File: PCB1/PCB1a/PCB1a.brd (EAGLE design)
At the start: 125.6 x 84.2 mm, 0 parts

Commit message: .
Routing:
- added copper zone on layer 1, net GND
- added copper zone on layer 16, net GND
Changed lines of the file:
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@@
 <setting verticaltext="up"/>
 </settings>
-<grid distance="3.75" unitdist="mm" unit="mm" style="lines" multiple="1" display="yes" altdistance="5" altunitdist="mil" altunit="mil"/>
+<grid distance="4" unitdist="mm" unit="mm" style="lines" multiple="1" display="yes" altdistance="5" altunitdist="mil" altunit="mil"/>
 <layers>
 <layer number="1" name="Top" color="4" fill="1" visible="yes" active="yes"/>
@@
 <layer number="51" name="tDocu" color="7" fill="1" visible="yes" active="yes"/>
 <layer number="52" name="bDocu" color="7" fill="1" visible="yes" active="yes"/>
+<layer number="91" name="Nets" color="2" fill="1" visible="no" active="no"/>
+<layer number="92" name="Busses" color="1" fill="1" visible="no" active="no"/>
+<layer number="93" name="Pins" color="2" fill="1" visible="no" active="no"/>
+<layer number="94" name="Symbols" color="4" fill="1" visible="no" active="no"/>
+<layer number="95" name="Names" color="7" fill="1" visible="no" active="no"/>
+<layer number="96" name="Values" color="7" fill="1" visible="no" active="no"/>
+<layer number="97" name="Info" color="7" fill="1" visible="no" active="no"/>
+<layer number="98" name="Guide" color="6" fill="1" visible="no" active="no"/>
 </layers>
 <board>
@@
 <dimension x1="50.6" y1="42.1" x2="50.6" y2="-42.1" x3="60.6" y3="0" textsize="1.778" layer="47"/>
 <dimension x1="50.6" y1="-42.1" x2="-75" y2="-42.1" x3="-12.2" y3="-52.1" textsize="1.778" layer="47"/>
+<rectangle x1="42.85" y1="34.35" x2="50.6" y2="42.1" layer="41"/>
+<rectangle x1="42.85" y1="34.35" x2="50.6" y2="42.1" layer="42"/>
 </plain>
 <attributes>
@@
 </elements>
 <signals>
-<signal name="S$1">
+<signal name="MOUNT2">
 <via x="46.85" y="38.35" extent="1-16" drill="3.2" diameter="7" locked="yes"/>
 <via x="46.85" y="-38.35" extent="1-16" drill="3.2" diameter="7" locked="yes"/>
@@
 <wire x1="-46.85" y1="38.35" x2="-46.85" y2="-38.35" width="0" layer="19" extent="1-1"/>
 </signal>
+<signal name="GND">
+<polygon width="0.1524" layer="1">
+<vertex x="50.6" y="-42.1"/>
+<vertex x="50.6" y="42.1"/>
+<vertex x="-75" y="42.1"/>
+<vertex x="-75" y="-42.1"/>
+</polygon>
+<polygon width="0.1524" layer="16">
+<vertex x="50.6" y="-42.1"/>
+<vertex x="50.6" y="42.1"/>
+<vertex x="-75" y="42.1"/>
+<vertex x="-75" y="-42.1"/>
+</polygon>
+</signal>
 </signals>

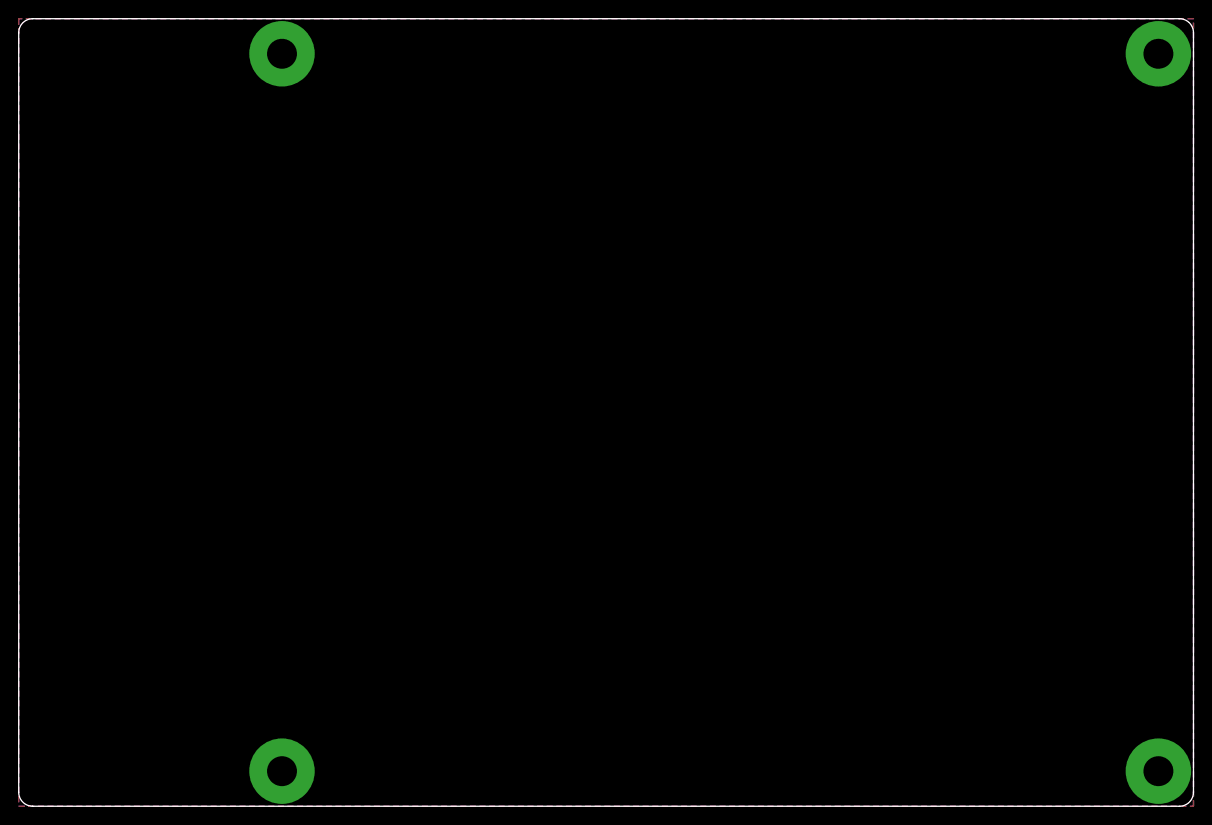
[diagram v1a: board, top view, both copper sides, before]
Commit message: Outline done .
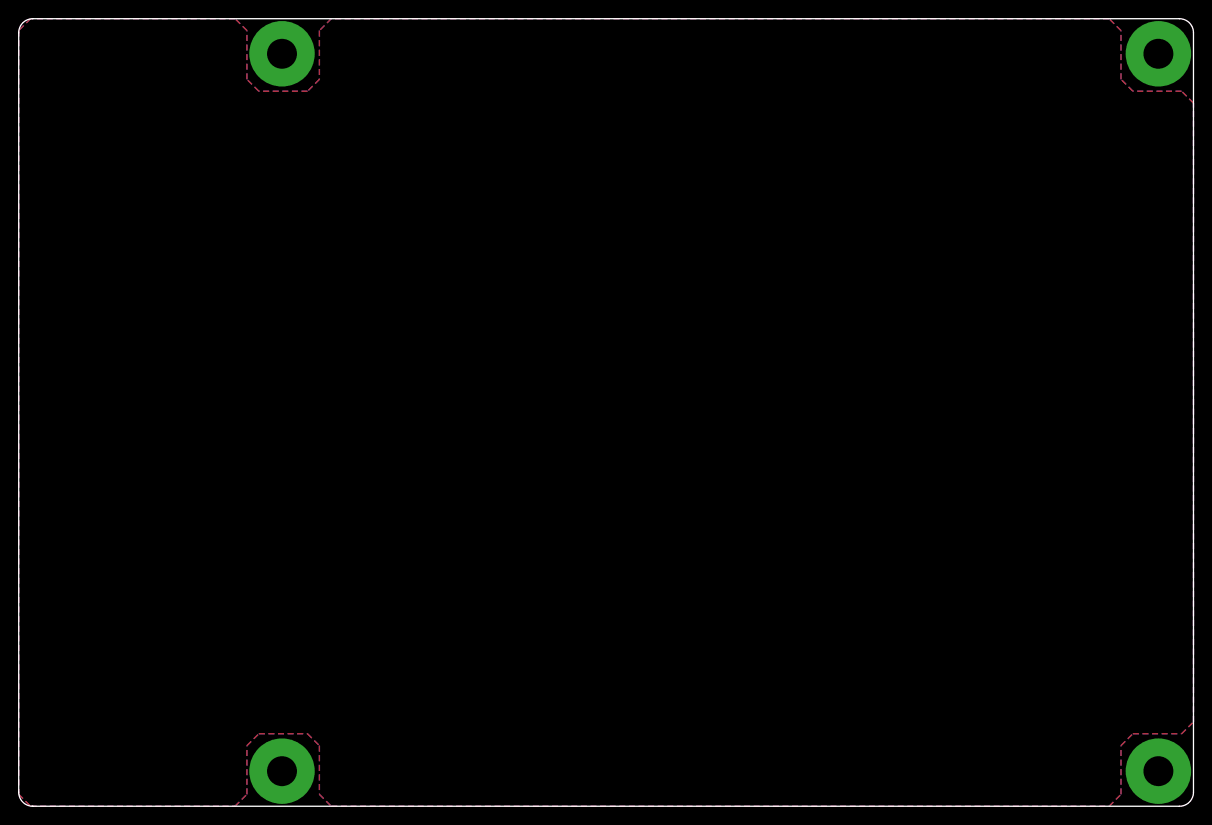
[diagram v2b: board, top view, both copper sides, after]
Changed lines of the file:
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@@
 <drawing>
 <settings>
-<setting alwaysvectorfont="no"/>
+<setting alwaysvectorfont="yes"/>
 <setting verticaltext="up"/>
 </settings>
@@
 <layer number="25" name="tNames" color="7" fill="1" visible="yes" active="yes"/>
 <layer number="26" name="bNames" color="7" fill="1" visible="yes" active="yes"/>
-<layer number="27" name="tValues" color="7" fill="1" visible="yes" active="yes"/>
-<layer number="28" name="bValues" color="7" fill="1" visible="yes" active="yes"/>
+<layer number="27" name="tValues" color="7" fill="1" visible="no" active="yes"/>
+<layer number="28" name="bValues" color="7" fill="1" visible="no" active="yes"/>
 <layer number="29" name="tStop" color="7" fill="3" visible="no" active="yes"/>
 <layer number="30" name="bStop" color="7" fill="6" visible="no" active="yes"/>
@@
 <layer number="41" name="tRestrict" color="4" fill="10" visible="yes" active="yes"/>
 <layer number="42" name="bRestrict" color="1" fill="10" visible="yes" active="yes"/>
-<layer number="43" name="vRestrict" color="2" fill="10" visible="yes" active="yes"/>
+<layer number="43" name="vRestrict" color="2" fill="10" visible="no" active="yes"/>
 <layer number="44" name="Drills" color="7" fill="1" visible="no" active="yes"/>
 <layer number="45" name="Holes" color="7" fill="1" visible="no" active="yes"/>
 <layer number="46" name="Milling" color="3" fill="1" visible="no" active="yes"/>
-<layer number="47" name="Measures" color="7" fill="1" visible="yes" active="yes"/>
-<layer number="48" name="Document" color="7" fill="1" visible="yes" active="yes"/>
-<layer number="49" name="Reference" color="7" fill="1" visible="yes" active="yes"/>
+<layer number="47" name="Measures" color="7" fill="1" visible="no" active="yes"/>
+<layer number="48" name="Document" color="7" fill="1" visible="no" active="yes"/>
+<layer number="49" name="Reference" color="7" fill="1" visible="no" active="yes"/>
 <layer number="51" name="tDocu" color="7" fill="1" visible="yes" active="yes"/>
 <layer number="52" name="bDocu" color="7" fill="1" visible="yes" active="yes"/>
@@
 <board>
 <plain>
-<wire x1="-75" y1="40.6" x2="-75" y2="-40.6" width="0" layer="20"/>
-<wire x1="-75" y1="-40.6" x2="-73.5" y2="-42.1" width="0" layer="20" curve="90"/>
-<wire x1="-73.5" y1="-42.1" x2="49.1" y2="-42.1" width="0" layer="20"/>
-<wire x1="-75" y1="40.6" x2="-73.5" y2="42.1" width="0" layer="20" curve="-90"/>
-<wire x1="49.1" y1="-42.1" x2="50.6" y2="-40.6" width="0" layer="20" curve="90"/>
-<wire x1="50.6" y1="-40.6" x2="50.6" y2="40.6" width="0" layer="20"/>
-<wire x1="50.6" y1="40.6" x2="49.1" y2="42.1" width="0" layer="20" curve="90"/>
-<wire x1="49.1" y1="42.1" x2="-73.5" y2="42.1" width="0" layer="20"/>
+<wire x1="-75" y1="40.6" x2="-75" y2="-40.6" width="0" layer="20" locked="yes"/>
+<wire x1="-75" y1="-40.6" x2="-73.5" y2="-42.1" width="0" layer="20" curve="90" locked="yes"/>
+<wire x1="-73.5" y1="-42.1" x2="49.1" y2="-42.1" width="0" layer="20" locked="yes"/>
+<wire x1="-75" y1="40.6" x2="-73.5" y2="42.1" width="0" layer="20" curve="-90" locked="yes"/>
+<wire x1="49.1" y1="-42.1" x2="50.6" y2="-40.6" width="0" layer="20" curve="90" locked="yes"/>
+<wire x1="50.6" y1="-40.6" x2="50.6" y2="40.6" width="0" layer="20" locked="yes"/>
+<wire x1="50.6" y1="40.6" x2="49.1" y2="42.1" width="0" layer="20" curve="90" locked="yes"/>
+<wire x1="49.1" y1="42.1" x2="-73.5" y2="42.1" width="0" layer="20" locked="yes"/>
 <dimension x1="-46.85" y1="-38.35" x2="46.85" y2="-38.35" x3="0" y3="-48.35" locked="yes" textsize="1.778" layer="47" visible="yes"/>
 <dimension x1="46.85" y1="38.35" x2="46.85" y2="-38.35" x3="56.85" y3="0" locked="yes" textsize="1.778" layer="47" visible="yes"/>
@@
 <dimension x1="50.6" y1="42.1" x2="50.6" y2="-42.1" x3="60.6" y3="0" textsize="1.778" layer="47"/>
 <dimension x1="50.6" y1="-42.1" x2="-75" y2="-42.1" x3="-12.2" y3="-52.1" textsize="1.778" layer="47"/>
-<rectangle x1="42.85" y1="34.35" x2="50.6" y2="42.1" layer="41"/>
-<rectangle x1="42.85" y1="34.35" x2="50.6" y2="42.1" layer="42"/>
 </plain>
 <attributes>
@@
 </elements>
 <signals>
+<signal name="MOUNT1">
+<via x="46.85" y="38.35" extent="1-16" drill="3.2" diameter="7" locked="yes"/>
+</signal>
 <signal name="MOUNT2">
-<via x="46.85" y="38.35" extent="1-16" drill="3.2" diameter="7" locked="yes"/>
 <via x="46.85" y="-38.35" extent="1-16" drill="3.2" diameter="7" locked="yes"/>
+</signal>
+<signal name="MOUNT3">
 <via x="-46.85" y="38.35" extent="1-16" drill="3.2" diameter="7" locked="yes"/>
+</signal>
+<signal name="MOUNT4">
 <via x="-46.85" y="-38.35" extent="1-16" drill="3.2" diameter="7" locked="yes"/>
-<wire x1="46.85" y1="-38.35" x2="46.85" y2="38.35" width="0" layer="19" extent="1-1"/>
-<wire x1="-46.85" y1="-38.35" x2="46.85" y2="-38.35" width="0" layer="19" extent="1-1"/>
-<wire x1="-46.85" y1="38.35" x2="-46.85" y2="-38.35" width="0" layer="19" extent="1-1"/>
 </signal>
 <signal name="GND">
+<polygon width="0.1524" layer="16">
+<vertex x="44.12" y="-34.35"/>
+<vertex x="49.33" y="-34.35"/>
+<vertex x="50.6" y="-33.08"/>
+<vertex x="50.6" y="33.08"/>
+<vertex x="49.33" y="34.35"/>
+<vertex x="44.12" y="34.35"/>
+<vertex x="42.85" y="35.62"/>
+<vertex x="42.85" y="40.83"/>
+<vertex x="41.58" y="42.1"/>
+<vertex x="-41.58" y="42.1"/>
+<vertex x="-42.85" y="40.83"/>
+<vertex x="-42.85" y="35.62"/>
+<vertex x="-44.12" y="34.35"/>
+<vertex x="-49.33" y="34.35"/>
+<vertex x="-50.6" y="35.62"/>
+<vertex x="-50.6" y="40.83"/>
+<vertex x="-51.87" y="42.1"/>
+<vertex x="-73.73" y="42.1"/>
+<vertex x="-75" y="40.83"/>
+<vertex x="-75" y="-40.83"/>
+<vertex x="-73.73" y="-42.1"/>
+<vertex x="-51.87" y="-42.1"/>
+<vertex x="-50.6" y="-40.83"/>
+<vertex x="-50.6" y="-35.62"/>
+<vertex x="-49.33" y="-34.35"/>
+<vertex x="-44.12" y="-34.35"/>
+<vertex x="-42.85" y="-35.62"/>
+<vertex x="-42.85" y="-40.83"/>
+<vertex x="-41.58" y="-42.1"/>
+<vertex x="41.58" y="-42.1"/>
+<vertex x="42.85" y="-40.83"/>
+<vertex x="42.85" y="-35.62"/>
+</polygon>
 <polygon width="0.1524" layer="1">
-<vertex x="50.6" y="-42.1"/>
-<vertex x="50.6" y="42.1"/>
-<vertex x="-75" y="42.1"/>
-<vertex x="-75" y="-42.1"/>
-</polygon>
-<polygon width="0.1524" layer="16">
-<vertex x="50.6" y="-42.1"/>
-<vertex x="50.6" y="42.1"/>
-<vertex x="-75" y="42.1"/>
-<vertex x="-75" y="-42.1"/>
+<vertex x="44.12" y="-34.35"/>
+<vertex x="49.33" y="-34.35"/>
+<vertex x="50.6" y="-33.08"/>
+<vertex x="50.6" y="33.08"/>
+<vertex x="49.33" y="34.35"/>
+<vertex x="44.12" y="34.35"/>
+<vertex x="42.85" y="35.62"/>
+<vertex x="42.85" y="40.83"/>
+<vertex x="41.58" y="42.1"/>
+<vertex x="-41.58" y="42.1"/>
+<vertex x="-42.85" y="40.83"/>
+<vertex x="-42.85" y="35.62"/>
+<vertex x="-44.12" y="34.35"/>
+<vertex x="-49.33" y="34.35"/>
+<vertex x="-50.6" y="35.62"/>
+<vertex x="-50.6" y="40.83"/>
+<vertex x="-51.87" y="42.1"/>
+<vertex x="-73.73" y="42.1"/>
+<vertex x="-75" y="40.83"/>
+<vertex x="-75" y="-40.83"/>
+<vertex x="-73.73" y="-42.1"/>
+<vertex x="-51.87" y="-42.1"/>
+<vertex x="-50.6" y="-40.83"/>
+<vertex x="-50.6" y="-35.62"/>
+<vertex x="-49.33" y="-34.35"/>
+<vertex x="-44.12" y="-34.35"/>
+<vertex x="-42.85" y="-35.62"/>
+<vertex x="-42.85" y="-40.83"/>
+<vertex x="-41.58" y="-42.1"/>
+<vertex x="41.58" y="-42.1"/>
+<vertex x="42.85" y="-40.83"/>
+<vertex x="42.85" y="-35.62"/>
 </polygon>
 </signal>
@@
 <mfgpreviewcolor name="substratecolor" color="0xFF786E46"/>
 </mfgpreviewcolors>
+<errors>
+</errors>
 </board>
 </drawing>
